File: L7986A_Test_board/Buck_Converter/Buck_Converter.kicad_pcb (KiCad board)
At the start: 2 copper layers, 17 parts, among them IC1 L7986A

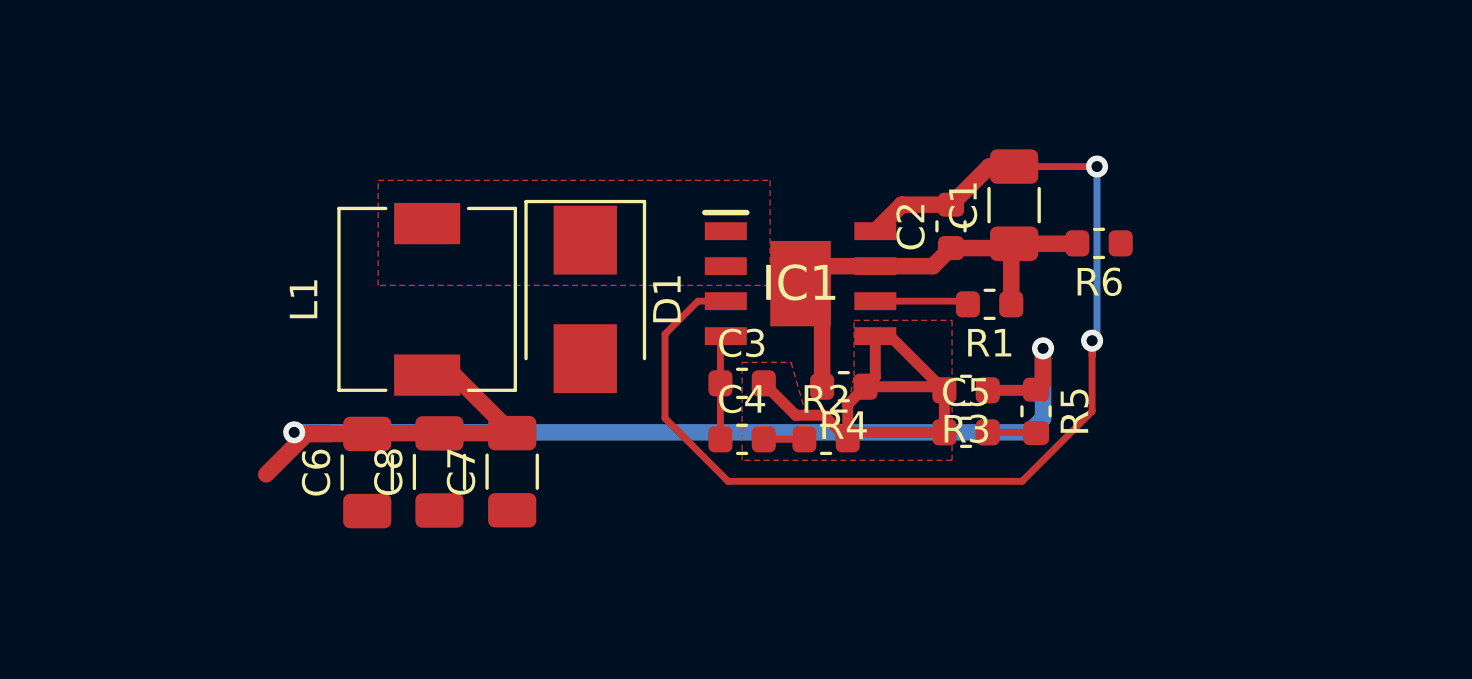
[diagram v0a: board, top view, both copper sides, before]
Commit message: Board zones added
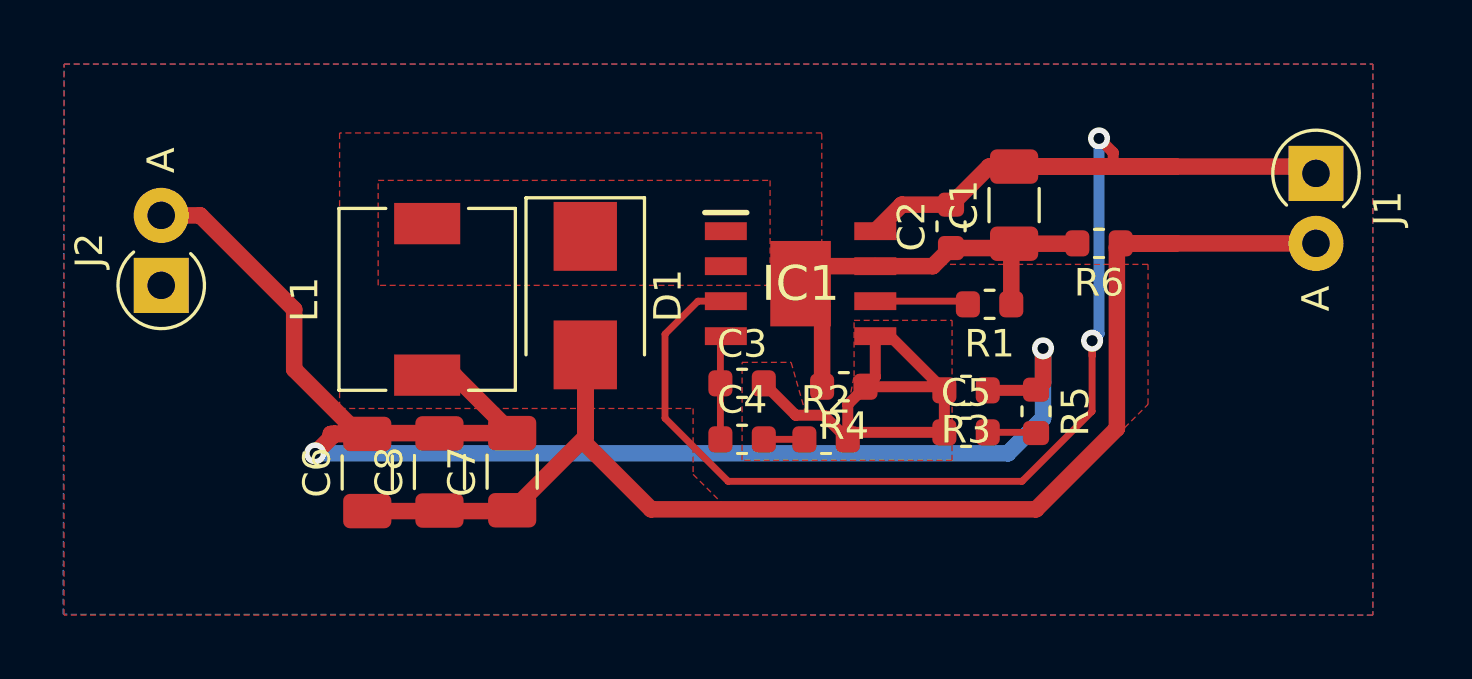
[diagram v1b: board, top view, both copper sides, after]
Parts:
- added J1: Conn_01x02_Male, Diode_THT:D_T-1_P2.54mm_Vertical_AnodeUp, F.Cu at (122.9, 61.5)
- added J2: Conn_01x02_Male, Diode_THT:D_T-1_P2.54mm_Vertical_AnodeUp, F.Cu at (81.0, 65.5)
- D1: value SK53 -> SK52
- moved D1 0.14 mm to (96.4, 65.9)
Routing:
- net GND: track 0.00 -> 52.6 mm
- net /VIN: track 41.8 -> 67.4 mm
- net /VOUT: track 48.2 -> 58.5 mm
- added copper zone on B.Cu, net GND
- added copper zone on F.Cu, net GND

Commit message: Filled zones fixed
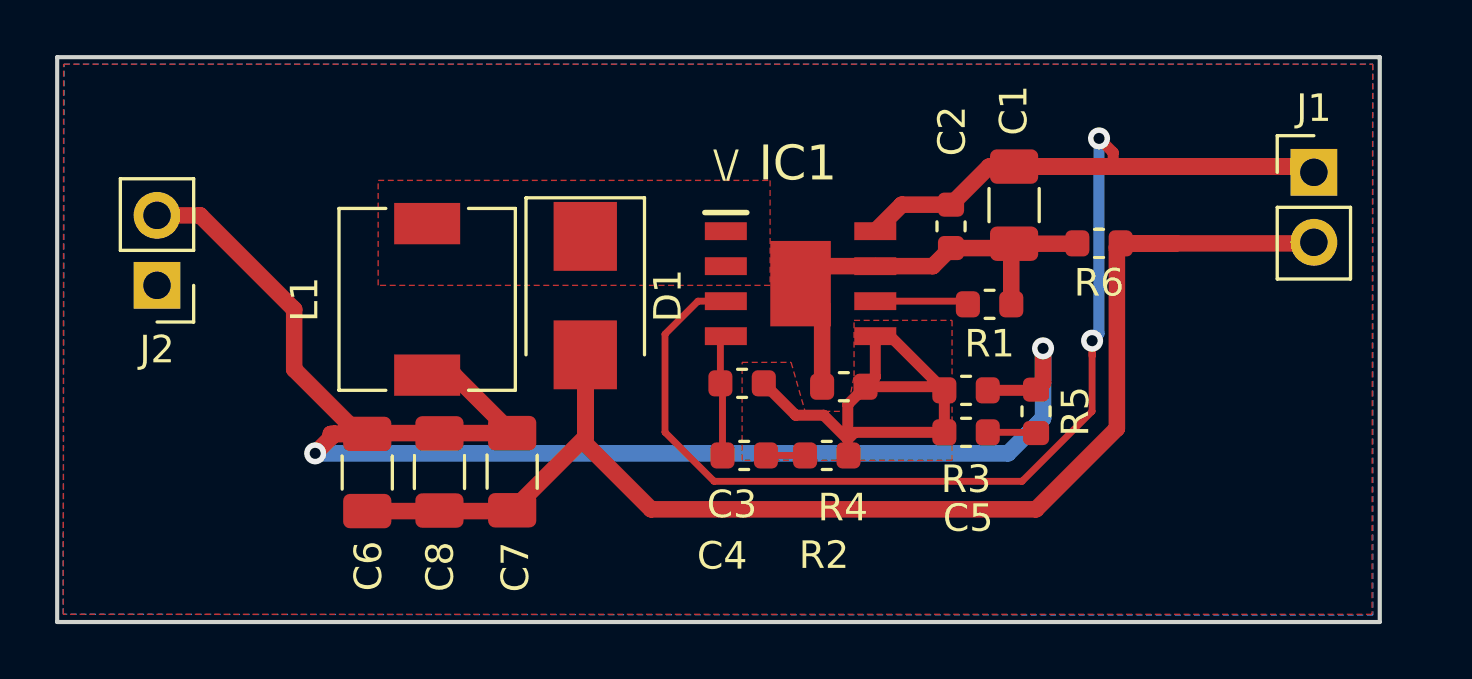
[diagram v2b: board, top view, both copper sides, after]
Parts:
- J1, J2: footprint Diode_THT:D_T-1_P2.54mm_Vertical_AnodeUp -> Connector_PinHeader_2.54mm:PinHeader_1x02_P2.54mm_Vertical
- moved C4 0.59 mm to (102.2, 71.7)
- moved R2 0.58 mm to (105.2, 71.7)
- moved J2 0.15 mm to (80.9, 65.5), turned to 180 degrees
- moved J1 0.09 mm to (122.9, 61.4), turned to 0 degrees
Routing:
- net /VIN: track 67.4 -> 78.7 mm
- net Net-(C3-Pad1): track 3.83 -> 4.44 mm
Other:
- board outline added: 48 x 20.5 mm
- board text added: "\/"

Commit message: Labels Fixed
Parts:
- moved J2 1.56 mm to (80.8, 64.0)
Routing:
- net /VOUT: track 58.9 -> 60.9 mm
- added copper zone on F.Cu, net BC_GND

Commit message: pre stiching
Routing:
- net GND: vias 0 -> 41
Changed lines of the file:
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@@
     (thickness 1.6)
     (drawings 5)
-    (tracks 98)
+    (tracks 139)
     (zones 0)
     (modules 19)
@@
   (layers
     (0 F.Cu signal)
-    (31 B.Cu signal hide)
+    (31 B.Cu signal)
     (32 B.Adhes user)
     (33 F.Adhes user)
@@
   )
   (setup
-    (last_trace_width 0.6)
+    (last_trace_width 0.25)
     (user_trace_width 0.4)
     (user_trace_width 0.6)
@@
   (segment (start 115.8495 64.008) (end 117.856 64.008) (width 0.6) (layer F.Cu) (net 1))
   (segment (start 115.8495 64.008) (end 122.936 64.008) (width 0.6) (layer F.Cu) (net 1))
+  (via (at 79.174999 59.174999) (size 0.8) (drill 0.4) (layers F.Cu B.Cu) (net 1))
+  (via (at 79.174999 66.174999) (size 0.8) (drill 0.4) (layers F.Cu B.Cu) (net 1))
+  (via (at 79.174999 70.174999) (size 0.8) (drill 0.4) (layers F.Cu B.Cu) (net 1))
+  (via (at 79.174999 74.174999) (size 0.8) (drill 0.4) (layers F.Cu B.Cu) (net 1))
+  (via (at 81.174999 68.174999) (size 0.8) (drill 0.4) (layers F.Cu B.Cu) (net 1))
+  (via (at 81.174999 72.174999) (size 0.8) (drill 0.4) (layers F.Cu B.Cu) (net 1))
+  (via (at 82.174999 75.174999) (size 0.8) (drill 0.4) (layers F.Cu B.Cu) (net 1))
+  (via (at 83.174999 59.174999) (size 0.8) (drill 0.4) (layers F.Cu B.Cu) (net 1))
+  (via (at 83.174999 65.174999) (size 0.8) (drill 0.4) (layers F.Cu B.Cu) (net 1))
+  (via (at 83.174999 70.174999) (size 0.8) (drill 0.4) (layers F.Cu B.Cu) (net 1))
+  (via (at 84.174999 73.174999) (size 0.8) (drill 0.4) (layers F.Cu B.Cu) (net 1))
+  (via (at 85.174999 61.174999) (size 0.8) (drill 0.4) (layers F.Cu B.Cu) (net 1))
+  (via (at 86.174999 75.174999) (size 0.8) (drill 0.4) (layers F.Cu B.Cu) (net 1))
+  (via (at 87.174999 59.174999) (size 0.8) (drill 0.4) (layers F.Cu B.Cu) (net 1))
+  (via (at 87.174999 63.174999) (size 0.8) (drill 0.4) (layers F.Cu B.Cu) (net 1))
+  (via (at 87.174999 67.174999) (size 0.8) (drill 0.4) (layers F.Cu B.Cu) (net 1))
+  (via (at 90.174999 60.174999) (size 0.8) (drill 0.4) (layers F.Cu B.Cu) (net 1))
+  (via (at 93.174999 59.174999) (size 0.8) (drill 0.4) (layers F.Cu B.Cu) (net 1))
+  (via (at 93.174999 67.174999) (size 0.8) (drill 0.4) (layers F.Cu B.Cu) (net 1))
+  (via (at 96.174999 60.174999) (size 0.8) (drill 0.4) (layers F.Cu B.Cu) (net 1))
+  (via (at 96.174999 74.174999) (size 0.8) (drill 0.4) (layers F.Cu B.Cu) (net 1))
+  (via (at 99.174999 59.174999) (size 0.8) (drill 0.4) (layers F.Cu B.Cu) (net 1))
+  (via (at 99.174999 75.174999) (size 0.8) (drill 0.4) (layers F.Cu B.Cu) (net 1))
+  (via (at 102.174999 60.174999) (size 0.8) (drill 0.4) (layers F.Cu B.Cu) (net 1))
+  (via (at 103.174999 75.174999) (size 0.8) (drill 0.4) (layers F.Cu B.Cu) (net 1))
+  (via (at 105.174999 59.174999) (size 0.8) (drill 0.4) (layers F.Cu B.Cu) (net 1))
+  (via (at 107.174999 61.174999) (size 0.8) (drill 0.4) (layers F.Cu B.Cu) (net 1))
+  (via (at 107.174999 75.174999) (size 0.8) (drill 0.4) (layers F.Cu B.Cu) (net 1))
+  (via (at 109.174999 59.174999) (size 0.8) (drill 0.4) (layers F.Cu B.Cu) (net 1))
+  (via (at 111.174999 75.174999) (size 0.8) (drill 0.4) (layers F.Cu B.Cu) (net 1))
+  (via (at 115.174999 74.174999) (size 0.8) (drill 0.4) (layers F.Cu B.Cu) (net 1))
+  (via (at 117.174999 59.174999) (size 0.8) (drill 0.4) (layers F.Cu B.Cu) (net 1))
+  (via (at 117.174999 66.174999) (size 0.8) (drill 0.4) (layers F.Cu B.Cu) (net 1))
+  (via (at 117.174999 70.174999) (size 0.8) (drill 0.4) (layers F.Cu B.Cu) (net 1))
+  (via (at 118.174999 73.174999) (size 0.8) (drill 0.4) (layers F.Cu B.Cu) (net 1))
+  (via (at 119.174999 68.174999) (size 0.8) (drill 0.4) (layers F.Cu B.Cu) (net 1))
+  (via (at 120.174999 71.174999) (size 0.8) (drill 0.4) (layers F.Cu B.Cu) (net 1))
+  (via (at 120.174999 75.174999) (size 0.8) (drill 0.4) (layers F.Cu B.Cu) (net 1))
+  (via (at 121.174999 66.174999) (size 0.8) (drill 0.4) (layers F.Cu B.Cu) (net 1))
+  (via (at 122.174999 69.174999) (size 0.8) (drill 0.4) (layers F.Cu B.Cu) (net 1))
+  (via (at 122.174999 73.174999) (size 0.8) (drill 0.4) (layers F.Cu B.Cu) (net 1))
   (segment (start 111.98 61.22) (end 114.99 61.22) (width 0.25) (layer F.Cu) (net 2))
   (via (at 114.81 67.54) (size 0.8) (drill 0.4) (layers F.Cu B.Cu) (net 2))
